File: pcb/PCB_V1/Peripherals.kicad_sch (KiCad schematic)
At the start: 32 parts, among them J301 SHT4x / XH 2.50, J302 FLOAT / 3.5 mm, J401 Molex 104031-0811, U301 DS3231MZ+TRL

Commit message: pcb: integrate reviewed parts and validate initial 100mm placement
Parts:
- BT301: footprint Battery:BatteryHolder_Keystone_3002_1x2032 -> Battery:BatteryHolder_MYOUNG_BS-07-A1BJ001_CR2032; LCSC (none) -> C2979167; MPN (none) -> BS-07-A1BJ001; Manufacturer (none) -> MYOUNG
- J302: footprint TerminalBlock_Phoenix:TerminalBlock_Phoenix_PT-1,5-2-3.5-H_1x02_P3.50mm_Horizontal -> GrowBox:TerminalBlock_DORABO_DB125-3.5_1x02_P3.50mm_Horizontal
- J401: LCSC (none) -> C585350; MPN (none) -> 1040310811; Manufacturer (none) -> Molex
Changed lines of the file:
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@@
 	(title_block
 		(title "03 - RTC / microSD / external sensors")
-		(date "2026-09-26")
-		(rev "0.16-DRAFT")
+		(date "2026-09-28")
+		(rev "0.17-DRAFT")
 		(company "GrowBox controller")
 		(comment 1 "Draft: input protection and LED drivers pending")
@@
 			)
 		)
-		(property "Footprint" "Battery:BatteryHolder_Keystone_3002_1x2032"
+		(property "Footprint" "Battery:BatteryHolder_MYOUNG_BS-07-A1BJ001_CR2032"
 			(at 134.62 68.58 0)
 			(hide yes)
@@
 			)
 		)
-		(property "Datasheet" ""
+		(property "Datasheet" "https://datasheet.lcsc.com/datasheet/pdf/fcfe81010ef1b91d8aa89bbdaa7da201.pdf"
 			(at 134.62 68.58 0)
 			(hide yes)
@@
 			)
 		)
+		(property "Manufacturer" "MYOUNG"
+			(at 134.62 68.58 0)
+			(hide yes)
+			(show_name no)
+			(do_not_autoplace no)
+			(effects
+				(font
+					(size 1 1)
+				)
+				(justify left)
+			)
+		)
+		(property "MPN" "BS-07-A1BJ001"
+			(at 134.62 68.58 0)
+			(hide yes)
+			(show_name no)
+			(do_not_autoplace no)
+			(effects
+				(font
+					(size 1 1)
+				)
+				(justify left)
+			)
+		)
+		(property "LCSC" "C2979167"
+			(at 134.62 68.58 0)
+			(hide yes)
+			(show_name no)
+			(do_not_autoplace no)
+			(effects
+				(font
+					(size 1 1)
+				)
+				(justify left)
+			)
+		)
 	)
 	(symbol
@@
 			)
 		)
-		(property "Footprint" "TerminalBlock_Phoenix:TerminalBlock_Phoenix_PT-1,5-2-3.5-H_1x02_P3.50mm_Horizontal"
+		(property "Footprint" "GrowBox:TerminalBlock_DORABO_DB125-3.5_1x02_P3.50mm_Horizontal"
 			(at 193.04 247.65 0)
 			(hide yes)
@@
 			)
 		)
-		(property "Datasheet" "https://www.hirose.com/en/product/document?clcode=&productname=&series=DM3&documenttype=Catalog&lang=en&documentid=D49662_en"
+		(property "Datasheet" "https://www.molex.com/content/dam/molex/molex-dot-com/products/automated/en-us/salesdrawingpdf/104/104031/1040310811_sd.pdf"
 			(at 370.84 73.66 0)
 			(hide yes)
@@
 			)
 		)
+		(property "Manufacturer" "Molex"
+			(at 370.84 73.66 0)
+			(hide yes)
+			(show_name no)
+			(do_not_autoplace no)
+			(effects
+				(font
+					(size 1 1)
+				)
+				(justify left)
+			)
+		)
+		(property "MPN" "1040310811"
+			(at 370.84 73.66 0)
+			(hide yes)
+			(show_name no)
+			(do_not_autoplace no)
+			(effects
+				(font
+					(size 1 1)
+				)
+				(justify left)
+			)
+		)
+		(property "LCSC" "C585350"
+			(at 370.84 73.66 0)
+			(hide yes)
+			(show_name no)
+			(do_not_autoplace no)
+			(effects
+				(font
+					(size 1 1)
+				)
+				(justify left)
+			)
+		)

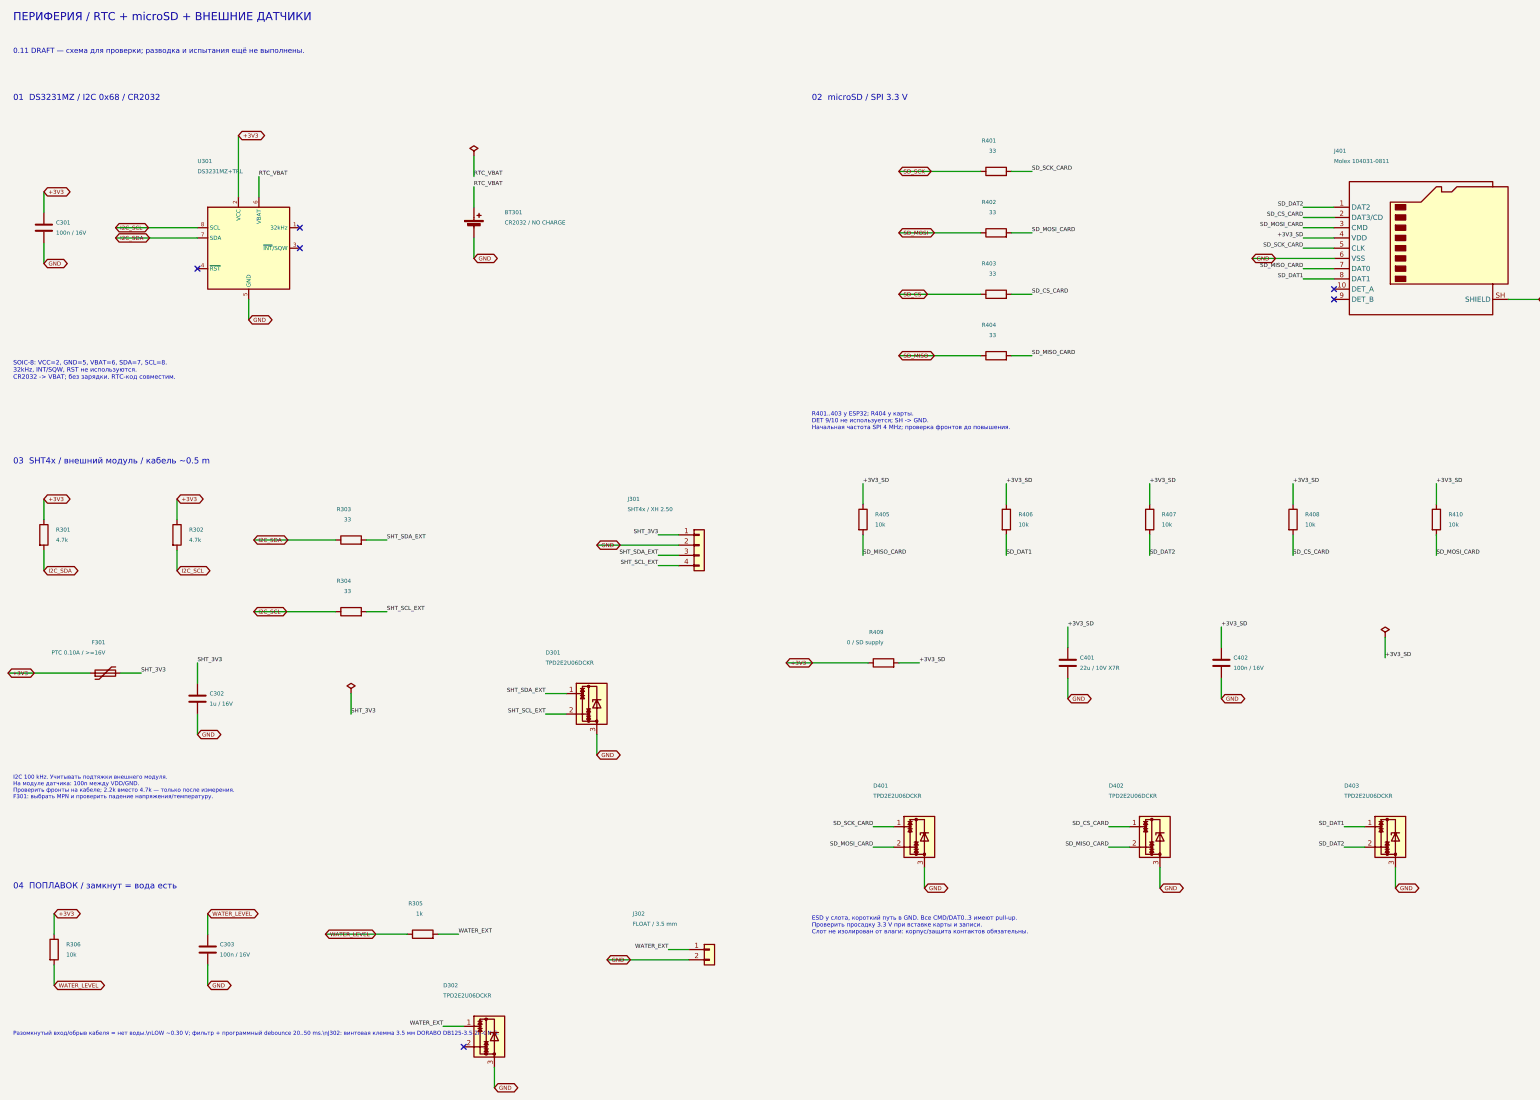
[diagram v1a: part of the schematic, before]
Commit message: pcb: simplify passives and microSD circuitry for revision 0.18
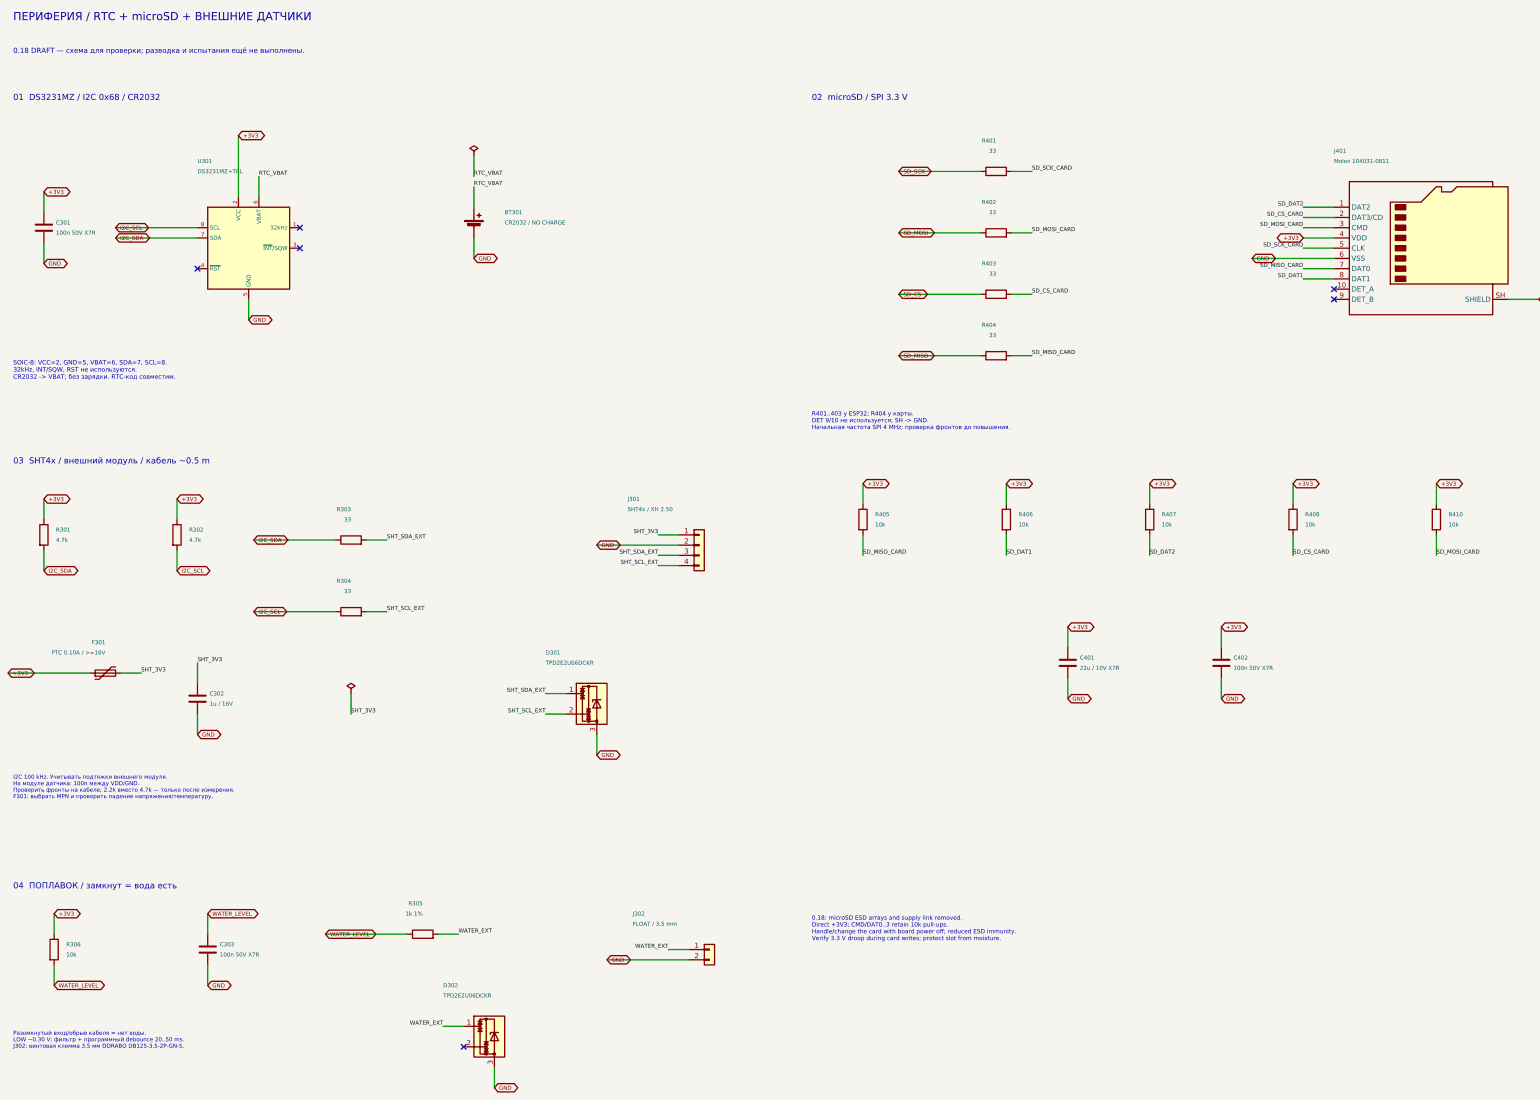
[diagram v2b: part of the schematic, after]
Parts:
- removed D401, D402, D403: TPD2E2U06DCKR, Package_TO_SOT_SMD:SOT-323_SC-70, symbol Power_Protection:TPD2E2U06DCK
- removed R409: 0 / SD supply, Resistor_SMD:R_0805_2012Metric, symbol Device:R
- C301, C303, C402: value 100n / 16V -> 100n 50V X7R; LCSC (none) -> C1591; MPN (none) -> CL10B104KB8NNNC; Manufacturer (none) -> Samsung
- R305: value 1k -> 1k 1%; LCSC (none) -> C21190; MPN (none) -> 0603WAF1001T5E; Manufacturer (none) -> UNI-ROYAL
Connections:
- net +3V3_SD is gone; now on net +3V3: C401.1, C402.1, J401.4 (VDD), R405.1, R406.1, R407.1, R408.1, R410.1
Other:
- note added: "0.18 DRAFT — схема для проверки; разводка и испытания ещё не выполнены."
- note added: "0.18: microSD ESD arrays and supply link removed. Direct +3V3; CMD/DAT0..3 retain 10k pull-ups. Handle/change the card with board power off; reduced ESD immunity. Verify 3.3 V droop during card writes; protect slot from moisture."
- note added: "Разомкнутый вход/обрыв кабеля = нет воды. LOW ~0.30 V; фильтр + программный debounce 20..50 ms. J302: винтовая клемма 3.5 мм DORABO DB125-3.5-2P-GN-S."
- note removed: "0.11 DRAFT — схема для проверки; разводка и испытания ещё не выполнены."
- note removed: "ESD у слота, короткий путь в GND. Все CMD/DAT0..3 имеют pull-up. Проверить просадку 3.3 V при вставке карты и записи. Слот не изолирован от влаги: корпус/защита контактов обязательны."
- note removed: "Разомкнутый вход/обрыв кабеля = нет воды.\nLOW ~0.30 V; фильтр + программный debounce 20..50 ms.\nJ302: винтовая клемма 3.5 мм DORABO DB125-3.5-2P-GN-S."
